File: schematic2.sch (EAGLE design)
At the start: 76 parts, among them IC6 DS3231/SO

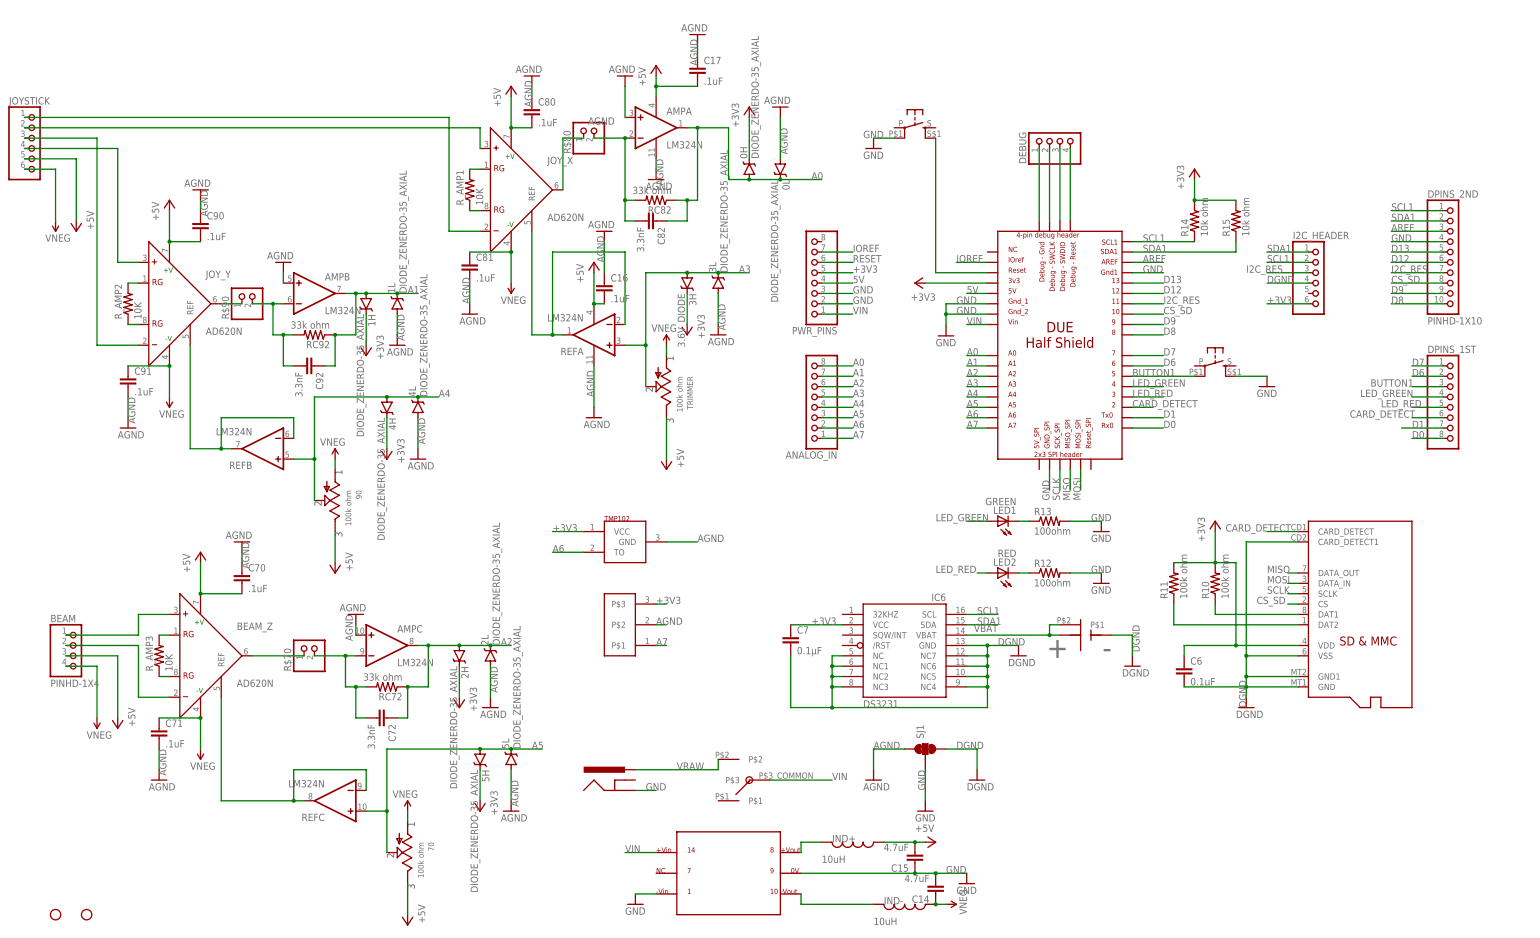
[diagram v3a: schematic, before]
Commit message: Finished routing top traces, started putting down silkscreen labels. Still need to deal with bottom ground plane.
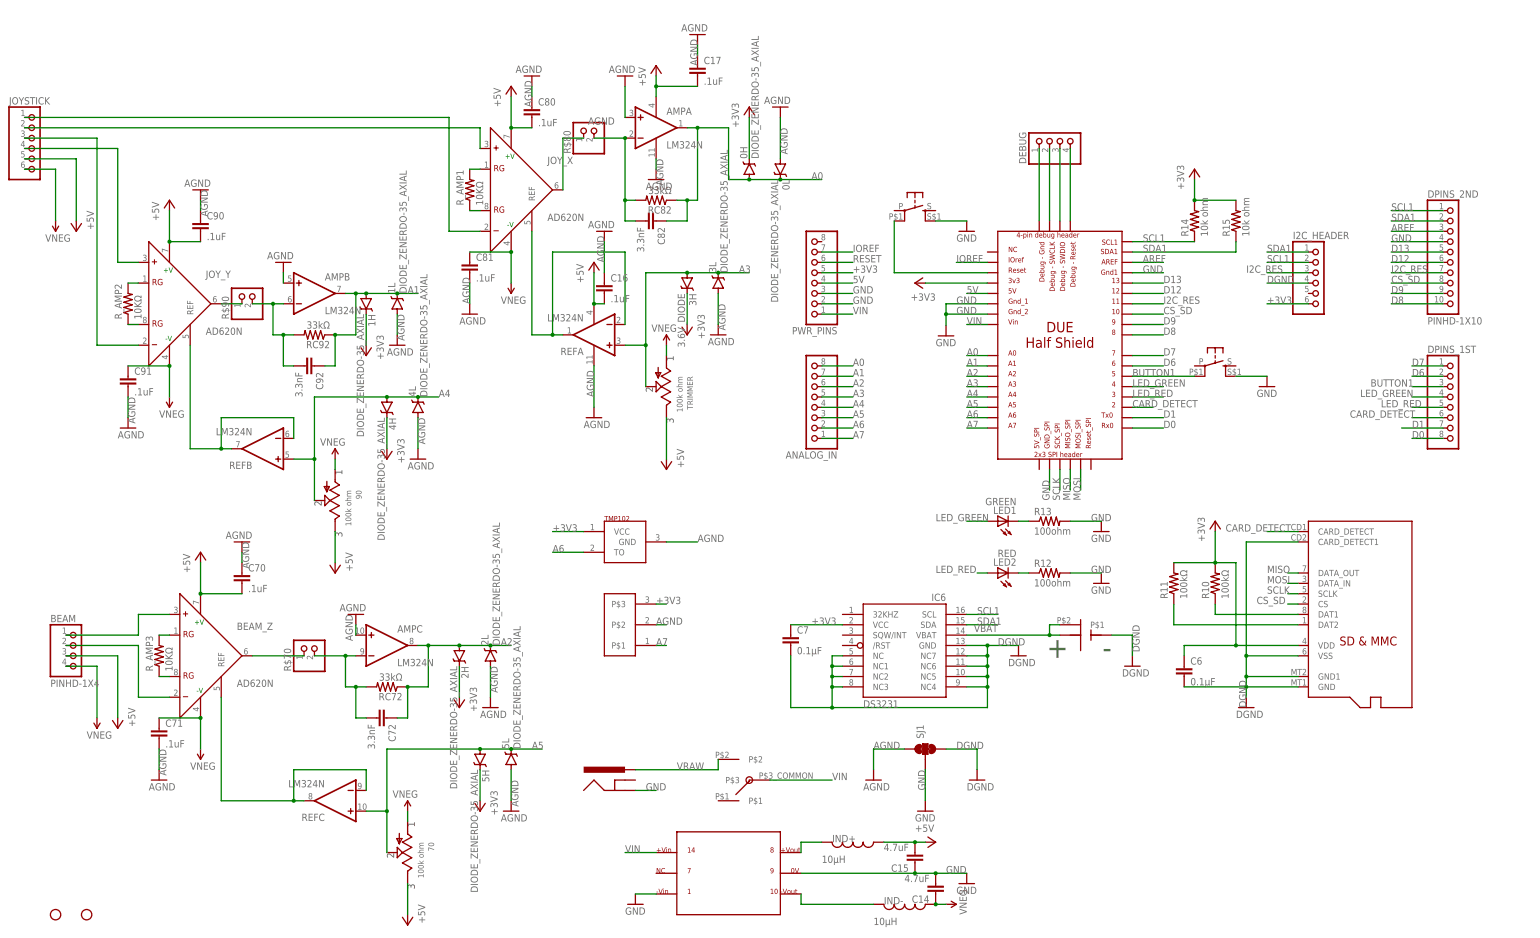
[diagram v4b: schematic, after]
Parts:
- IND+, IND-: value 10uH -> 10µH
- R10, R11: value 100k ohm -> 100kΩ
- RC72, RC82, RC92: value 33k ohm -> 33kΩ
- RESET: value PUSHBUTTON_DPST_SMD -> PUSHBUTTON
- R_AMP1, R_AMP2, R_AMP3: value 10K -> 10KΩ
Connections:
- net GND: now also RESET.S1; no longer RESET.P1
- net RESET: now also RESET.P1; no longer RESET.S1
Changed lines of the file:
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@@
 <part name="C92" library="Felicia_force_logger" deviceset="CAP" device="0805" value="3.3nF"/>
 <part name="C82" library="Felicia_force_logger" deviceset="CAP" device="0805" value="3.3nF"/>
-<part name="R_AMP2" library="Felicia_force_logger" deviceset="RESISTOR_SMD" device="R0805" value="10K"/>
-<part name="R_AMP1" library="Felicia_force_logger" deviceset="RESISTOR_SMD" device="R0805" value="10K"/>
-<part name="R_AMP3" library="Felicia_force_logger" deviceset="RESISTOR_SMD" device="R0805" value="10K"/>
+<part name="R_AMP2" library="Felicia_force_logger" deviceset="RESISTOR_SMD" device="R0805" value="10KΩ"/>
+<part name="R_AMP1" library="Felicia_force_logger" deviceset="RESISTOR_SMD" device="R0805" value="10KΩ"/>
+<part name="R_AMP3" library="Felicia_force_logger" deviceset="RESISTOR_SMD" device="R0805" value="10KΩ"/>
 <part name="U$3" library="Felicia_force_logger" deviceset="DC-DC_CONVERTER_DUAL_SUPPLY" device=""/>
 <part name="GND7" library="Felicia_force_logger" deviceset="GND" device=""/>
@@
 <part name="C15" library="Felicia_force_logger" deviceset="CAP" device="0805" value="4.7uF"/>
 <part name="C14" library="Felicia_force_logger" deviceset="CAP" device="0805" value="4.7uF"/>
-<part name="IND+" library="Felicia_force_logger" deviceset="INDUCTOR" device="0805_TY" value="10uH"/>
-<part name="IND-" library="Felicia_force_logger" deviceset="INDUCTOR" device="0805_TY" value="10uH"/>
+<part name="IND+" library="Felicia_force_logger" deviceset="INDUCTOR" device="0805_TY" value="10µH"/>
+<part name="IND-" library="Felicia_force_logger" deviceset="INDUCTOR" device="0805_TY" value="10µH"/>
 <part name="U$11" library="Felicia_force_logger" deviceset="MICROSD" device=""/>
 <part name="IC6" library="Felicia_force_logger" deviceset="DS3231" device="/SO"/>
@@
 <part name="GND17" library="Felicia_force_logger" deviceset="DGND" device=""/>
 <part name="GND18" library="Felicia_force_logger" deviceset="DGND" device=""/>
-<part name="R10" library="Felicia_force_logger" deviceset="RESISTOR_SMD" device="R0805" value="100k ohm"/>
-<part name="R11" library="Felicia_force_logger" deviceset="RESISTOR_SMD" device="R0805" value="100k ohm"/>
+<part name="R10" library="Felicia_force_logger" deviceset="RESISTOR_SMD" device="R0805" value="100kΩ"/>
+<part name="R11" library="Felicia_force_logger" deviceset="RESISTOR_SMD" device="R0805" value="100kΩ"/>
 <part name="+3V8" library="supply1" deviceset="+3V3" device=""/>
 <part name="C6" library="Felicia_force_logger" deviceset="CAP" device="0805" value="0.1µF"/>
@@
 <part name="+3V9" library="supply1" deviceset="+3V3" device=""/>
 <part name="INPUT" library="Felicia_force_logger" deviceset="PUSHBUTTON_DPST_SMD" device=""/>
-<part name="RESET" library="Felicia_force_logger" deviceset="PUSHBUTTON_DPST_SMD" device=""/>
+<part name="RESET" library="Felicia_force_logger" deviceset="PUSHBUTTON_DPST_SMD" device="" value="PUSHBUTTON"/>
 <part name="GND25" library="Felicia_force_logger" deviceset="GND" device=""/>
 <part name="DEBUG" library="Felicia_force_logger" deviceset="PINHD-1X4" device="LOCK"/>
@@
 <part name="GND37" library="Felicia_force_logger" deviceset="GND" device=""/>
 <part name="GND22" library="Felicia_force_logger" deviceset="GND" device=""/>
-<part name="RC92" library="Felicia_force_logger" deviceset="RESISTOR_SMD" device="R0805" value="33k ohm"/>
-<part name="RC82" library="Felicia_force_logger" deviceset="RESISTOR_SMD" device="R0805" value="33k ohm"/>
-<part name="RC72" library="Felicia_force_logger" deviceset="RESISTOR_SMD" device="R0805" value="33k ohm"/>
+<part name="RC92" library="Felicia_force_logger" deviceset="RESISTOR_SMD" device="R0805" value="33kΩ"/>
+<part name="RC82" library="Felicia_force_logger" deviceset="RESISTOR_SMD" device="R0805" value="33kΩ"/>
+<part name="RC72" library="Felicia_force_logger" deviceset="RESISTOR_SMD" device="R0805" value="33kΩ"/>
 <part name="STANDOFF1" library="miller" deviceset="STAND-OFF" device=""/>
 <part name="STANDOFF2" library="miller" deviceset="STAND-OFF" device=""/>
@@
 <instance part="+3V9" gate="G$1" x="284.48" y="187.96"/>
 <instance part="INPUT" gate="G$1" x="289.56" y="137.16"/>
-<instance part="RESET" gate="G$1" x="215.9" y="195.58"/>
-<instance part="GND25" gate="1" x="205.74" y="193.04"/>
+<instance part="RESET" gate="G$1" x="215.9" y="175.26"/>
+<instance part="GND25" gate="1" x="228.6" y="172.72"/>
 <instance part="DEBUG" gate="G$1" x="251.46" y="195.58" rot="R90"/>
 <instance part="U$28" gate="G$1" x="144.78" y="33.02"/>
@@
 </segment>
 <segment>
-<pinref part="RESET" gate="G$1" pin="P1"/>
-<pinref part="GND25" gate="1" pin="GND"/>
-<wire x1="210.82" y1="195.58" x2="205.74" y2="195.58" width="0.1524" layer="91"/>
-<label x="203.2" y="195.58" size="1.778" layer="95"/>
-</segment>
-<segment>
 <pinref part="U$1" gate="G$1" pin="GND1"/>
 <wire x1="269.24" y1="162.56" x2="276.86" y2="162.56" width="0.1524" layer="91"/>
@@
 <pinref part="GND22" gate="1" pin="GND"/>
 </segment>
+<segment>
+<pinref part="RESET" gate="G$1" pin="S1"/>
+<wire x1="220.98" y1="175.26" x2="228.6" y2="175.26" width="0.1524" layer="91"/>
+<pinref part="GND25" gate="1" pin="GND"/>
+</segment>
 </net>
 <net name="CARD_DETECT" class="0">
@@
 <segment>
 <pinref part="U$1" gate="G$1" pin="RESET"/>
-<pinref part="RESET" gate="G$1" pin="S1"/>
-<wire x1="233.68" y1="162.56" x2="220.98" y2="162.56" width="0.1524" layer="91"/>
-<wire x1="220.98" y1="162.56" x2="220.98" y2="195.58" width="0.1524" layer="91"/>
-</segment>
-</net>
+<wire x1="233.68" y1="162.56" x2="210.82" y2="162.56" width="0.1524" layer="91"/>
+<pinref part="RESET" gate="G$1" pin="P1"/>
+<wire x1="210.82" y1="175.26" x2="210.82" y2="162.56" width="0.1524" layer="91"/>
+</segment>
+</net>
